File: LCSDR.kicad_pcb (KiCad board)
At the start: 2 copper layers, 100 x 95 mm, 196 parts, among them J1 Conn_01x10, J10 Conn_01x01, J11 Conn_01x01, J2 Conn_01x10, J3 phones, J4 MIC_PTT, J5 Conn_01x10, J6 Conn_Coaxial, J7 Conn_01x10, J8 Conn_01x01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

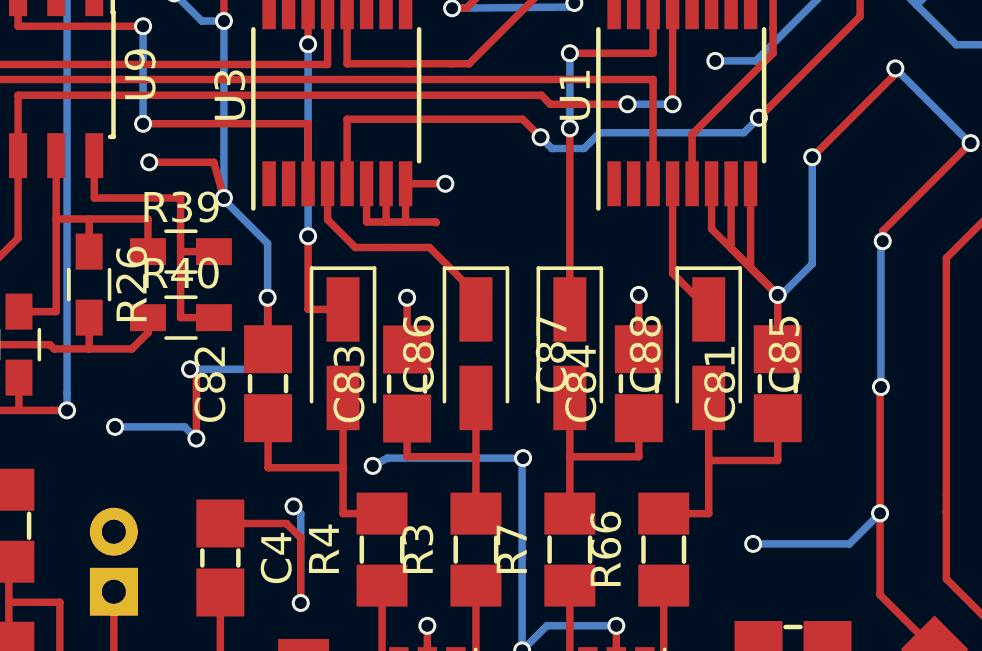
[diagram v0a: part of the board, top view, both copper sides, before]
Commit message: fix PCB distance, right after mixer
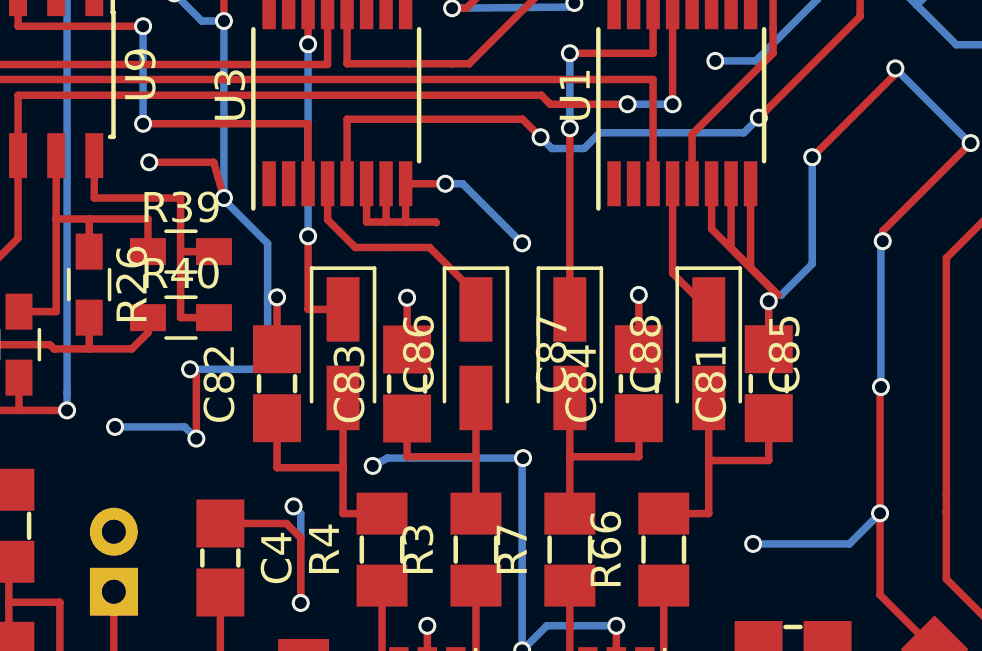
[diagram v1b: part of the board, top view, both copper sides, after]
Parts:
- moved C81 0.30 mm to (180.1, 105.1)
- moved C82 0.30 mm to (163.7, 105.1)
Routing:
- net GND: track 1138.4 -> 1142.1 mm, vias 265 -> 266
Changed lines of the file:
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@@
     (links 414)
     (no_connects 0)
-    (area 114.949999 39.949999 215.050001 135.050001)
+    (area 114.135 38.25238 219.055 136.747619)
     (thickness 1.6)
     (drawings 8)
-    (tracks 1935)
+    (tracks 1939)
     (zones 0)
     (modules 196)
@@
   )
   (module UI:C_1206_0603 (layer F.Cu)
-    (at 180.43 105.14 90)
+    (at 180.13 105.14 90)
     (descr "Capacitor SMD 0603, reflow soldering, AVX (see smccp.pdf)")
     (tags "capacitor 0603")
@@
   )
   (module UI:C_1206_0603 (layer F.Cu)
-    (at 163.44 105.14 90)
+    (at 163.74 105.14 90)
     (descr "Capacitor SMD 0603, reflow soldering, AVX (see smccp.pdf)")
     (tags "capacitor 0603")
@@
   (gr_line (start 116.5 62) (end 116.5 48) (angle 90) (layer Edge.Cuts) (width 0.1))
   (gr_line (start 115 62) (end 116.5 62) (angle 90) (layer Edge.Cuts) (width 0.1))
+  (segment (start 169.35 98.475) (end 169.925 98.475) (width 0.25) (layer B.Cu) (net 1))
+  (via (at 169.35 98.475) (size 0.6) (drill 0.4) (layers F.Cu B.Cu) (net 1))
+  (segment (start 168.025 98.475) (end 169.35 98.475) (width 0.25) (layer F.Cu) (net 1))
+  (via (at 171.91 100.46) (size 0.6) (drill 0.4) (layers F.Cu B.Cu) (net 1))
+  (segment (start 169.925 98.475) (end 171.91 100.46) (width 0.25) (layer B.Cu) (net 1))
+  (segment (start 180.13 103.99) (end 180.13 102.39) (width 0.25) (layer F.Cu) (net 1) (status 400000))
+  (segment (start 180.34 102.18) (end 180.55 102.18) (width 0.25) (layer B.Cu) (net 1))
+  (segment (start 180.13 102.39) (end 180.34 102.18) (width 0.25) (layer B.Cu) (net 1))
+  (via (at 180.13 102.39) (size 0.6) (drill 0.4) (layers F.Cu B.Cu) (net 1))
+  (segment (start 163.74 103.99) (end 163.74 102.26) (width 0.25) (layer F.Cu) (net 1) (status 400000))
+  (via (at 163.74 102.26) (size 0.6) (drill 0.4) (layers F.Cu B.Cu) (net 1))
   (segment (start 180 43) (end 175.45 43) (width 0.25) (layer B.Cu) (net 1))
   (via (at 163.8 46.8) (size 0.6) (drill 0.4) (layers F.Cu B.Cu) (net 1))
@@
   (segment (start 183.84 112.18) (end 185.656827 113.996827) (width 0.25) (layer F.Cu) (net 1))
   (segment (start 180.43 102.18) (end 180.55 102.18) (width 0.25) (layer B.Cu) (net 1))
-  (via (at 180.43 102.18) (size 0.6) (drill 0.4) (layers F.Cu B.Cu) (net 1))
   (segment (start 179.63 110.5) (end 179.69 110.5) (width 0.25) (layer F.Cu) (net 1))
   (segment (start 179.61 110.48) (end 179.63 110.5) (width 0.25) (layer F.Cu) (net 1))
@@
   (segment (start 178.875 100.625) (end 180.43 102.18) (width 0.25) (layer F.Cu) (net 1))
   (segment (start 178.225 98.475) (end 178.225 99.985) (width 0.25) (layer F.Cu) (net 1))
-  (segment (start 180.43 102.18) (end 180.43 103.99) (width 0.25) (layer F.Cu) (net 1))
   (segment (start 180.42 102.18) (end 180.43 102.18) (width 0.25) (layer F.Cu) (net 1))
   (segment (start 178.225 99.985) (end 180.42 102.18) (width 0.25) (layer F.Cu) (net 1))
@@
   (via (at 161.97 93.05) (size 0.6) (drill 0.4) (layers F.Cu B.Cu) (net 1))
   (segment (start 163.425 102.275) (end 163.425 100.465) (width 0.25) (layer B.Cu) (net 1))
-  (segment (start 163.44 102.29) (end 163.425 102.275) (width 0.25) (layer F.Cu) (net 1))
-  (via (at 163.425 102.275) (size 0.6) (drill 0.4) (layers F.Cu B.Cu) (net 1))
-  (segment (start 163.44 103.99) (end 163.44 102.29) (width 0.25) (layer F.Cu) (net 1))
   (segment (start 159.48 97.76) (end 159.48 97.7) (width 0.25) (layer B.Cu) (net 1))
   (via (at 159.48 97.76) (size 0.6) (drill 0.4) (layers F.Cu B.Cu) (net 1))
@@
   (segment (start 168.075 104) (end 168.075 102.275) (width 0.25) (layer F.Cu) (net 1))
   (via (at 168.075 102.275) (size 0.6) (drill 0.4) (layers F.Cu B.Cu) (net 1))
-  (segment (start 168.025 98.475) (end 169.35 98.475) (width 0.25) (layer F.Cu) (net 1))
-  (via (at 169.35 98.475) (size 0.6) (drill 0.4) (layers F.Cu B.Cu) (net 1))
   (segment (start 168.025 98.475) (end 168.025 99.75) (width 0.25) (layer F.Cu) (net 1))
   (segment (start 167.375 99.75) (end 168.025 99.75) (width 0.25) (layer F.Cu) (net 1))
@@
   (segment (start 165.425 94.5) (end 152.5675 94.5) (width 0.25) (layer F.Cu) (net 26))
   (segment (start 165.425 92.575) (end 165.425 94.5) (width 0.25) (layer F.Cu) (net 26))
-  (segment (start 180.43 107.7) (end 178.13 107.7) (width 0.25) (layer F.Cu) (net 27))
-  (segment (start 180.43 106.29) (end 180.43 107.7) (width 0.25) (layer F.Cu) (net 27))
+  (segment (start 180.13 106.29) (end 180.13 107.7) (width 0.25) (layer F.Cu) (net 27))
+  (segment (start 180.13 107.7) (end 178.13 107.7) (width 0.25) (layer F.Cu) (net 27))
   (segment (start 176.63 109.47) (end 178.13 109.47) (width 0.25) (layer F.Cu) (net 27))
   (segment (start 178.13 107.7) (end 178.13 109.47) (width 0.25) (layer F.Cu) (net 27))
@@
   (via (at 159.275 96.475) (size 0.6) (drill 0.4) (layers F.Cu B.Cu) (net 28))
   (segment (start 155.1075 92.1375) (end 155.1075 93.225) (width 0.25) (layer F.Cu) (net 28))
-  (segment (start 163.44 106.29) (end 163.44 107.94) (width 0.25) (layer F.Cu) (net 29))
-  (segment (start 165.94 107.94) (end 163.44 107.94) (width 0.25) (layer F.Cu) (net 29))
+  (segment (start 163.74 106.29) (end 163.74 107.94) (width 0.25) (layer F.Cu) (net 29))
+  (segment (start 165.94 107.94) (end 163.74 107.94) (width 0.25) (layer F.Cu) (net 29))
   (segment (start 165.94 105.615) (end 165.94 107.94) (width 0.25) (layer F.Cu) (net 29))
   (segment (start 165.94 107.94) (end 165.94 109.47) (width 0.25) (layer F.Cu) (net 29))

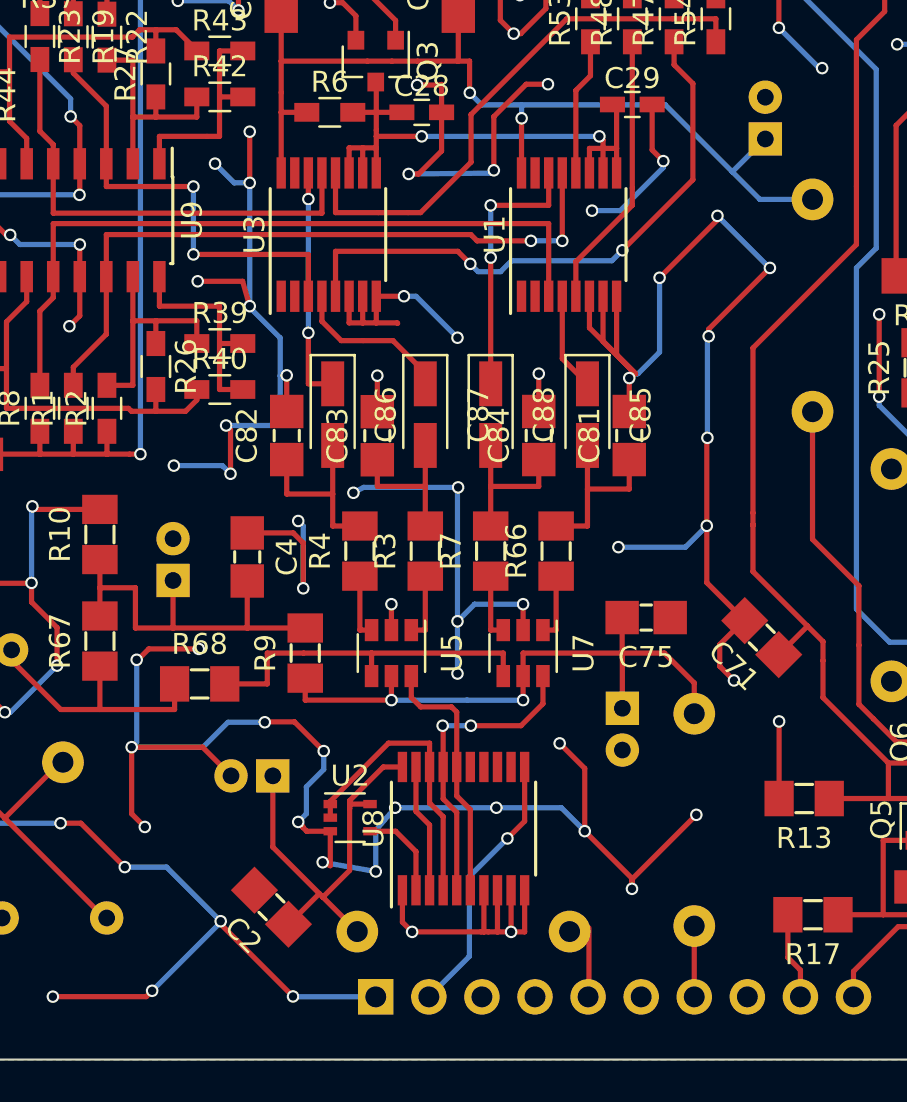
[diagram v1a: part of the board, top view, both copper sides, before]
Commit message: rotate phase with 74LVC74APW
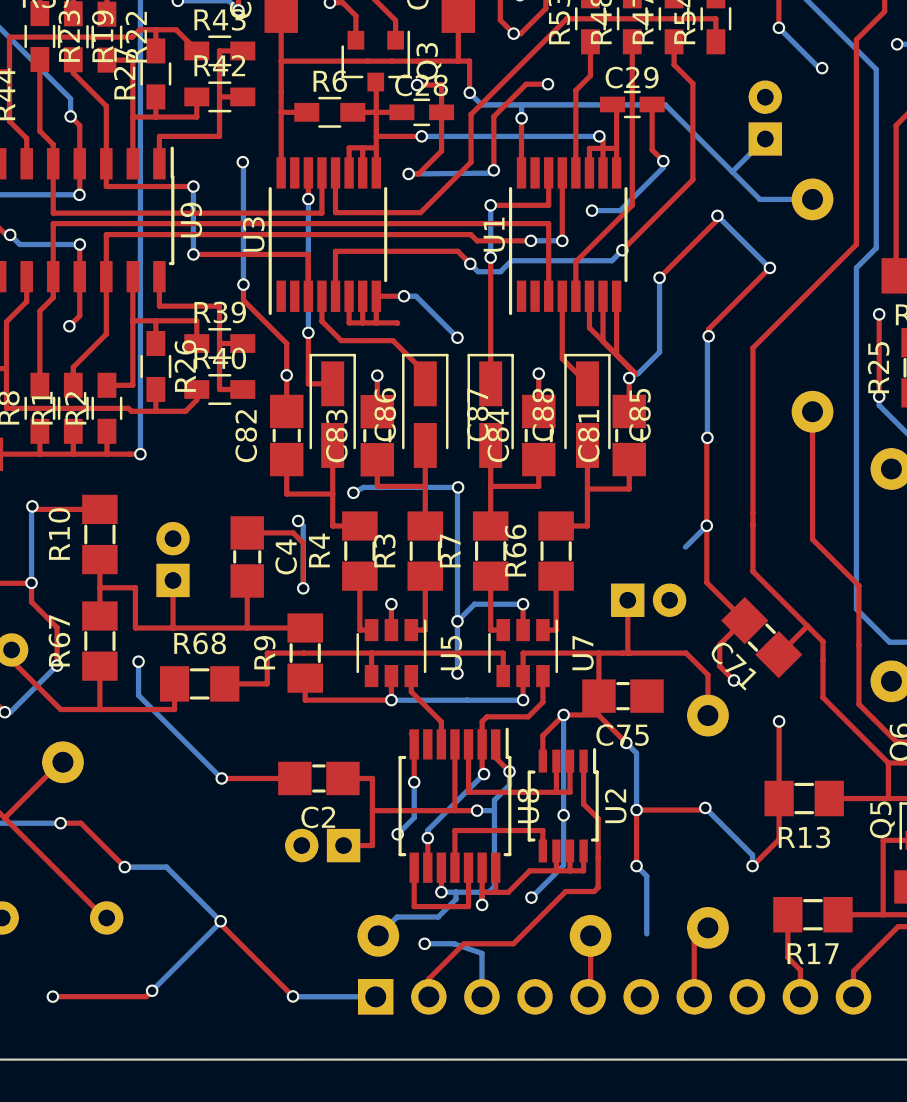
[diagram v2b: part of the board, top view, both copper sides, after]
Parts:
- U2: value 74LVC1G00DCKR -> 74LVC1G74; footprint TO_SOT_Packages_SMD:SOT-353_SC-70-5 -> Housings_SSOP:TSSOP-8_3x3mm_Pitch0.65mm
- U8: value 74LCX574 -> 74LS74; footprint Housings_SSOP:TSSOP-20_4.4x6.5mm_Pitch0.65mm -> Housings_SSOP:TSSOP-14_4.4x5mm_Pitch0.65mm
- moved U2 10.2 mm to (177.0, 122.9), turned to 270 degrees
- moved C2 6.56 mm to (165.3, 121.5), turned to 180 degrees
- moved C76 5.18 mm to (180.1, 113.0), turned to 0 degrees
- moved C3 4.75 mm to (166.5, 124.8)
- moved C75 3.92 mm to (179.8, 117.6)
- moved U8 1.16 mm to (171.8, 122.9), turned to 270 degrees
- moved L1 1.03 mm to (173.3, 129.1)
- moved L10 0.66 mm to (183.9, 123.7)
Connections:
- U2 pad 1: Net-(U2-Pad1) -> CLK
- U2 pad 2: Net-(U2-Pad1) -> Net-(U2-Pad2)
- U2 pad 3: GND -> Net-(U2-Pad2)
- U2 pad 4: Net-(U2-Pad4) -> GND
- U2 pad 5: VCC -> Net-(U2-Pad5)
- U8 pad 1: GND -> VCC
- U8 pad 10: GND -> VCC
- U8 pad 11: CLK -> Net-(U2-Pad5)
- U8 pad 12: (no net) -> Net-(U8-Pad12)
- U8 pad 13: (no net) -> VCC
- U8 pad 14: (no net) -> VCC
- U8 pad 2: Net-(U2-Pad4) -> P90
- U8 pad 3: Net-(U8-Pad19) -> Net-(U2-Pad2)
- U8 pad 4: Net-(U2-Pad1) -> VCC
- U8 pad 5: P90 -> P0
- U8 pad 6: P0 -> (no net)
- U8 pad 8: GND -> Net-(U8-Pad12)
- U8 pad 9: GND -> P90
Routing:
- net GND: track 1142.1 -> 1099.1 mm, vias 266 -> 255
- net VCC: track 21.3 -> 42.7 mm, vias 0 -> 4
- net Net-(U2-Pad1): track 14.0 -> 0.00 mm
- net Net-(U2-Pad2): track 0.00 -> 10.1 mm
- net P0: track 12.3 -> 3.87 mm
- net Net-(U2-Pad5): track 0.00 -> 6.96 mm
- net Net-(U8-Pad12): track 0.00 -> 6.32 mm
- net Net-(U8-Pad19): track 6.17 -> 0.00 mm
- net Net-(U2-Pad4): track 4.45 -> 0.00 mm
- net CLK: track 13.5 -> 17.7 mm, vias 1 -> 0
- net P90: track 14.7 -> 12.7 mm
- net Net-(C75-Pad2): track 29.5 -> 30.9 mm

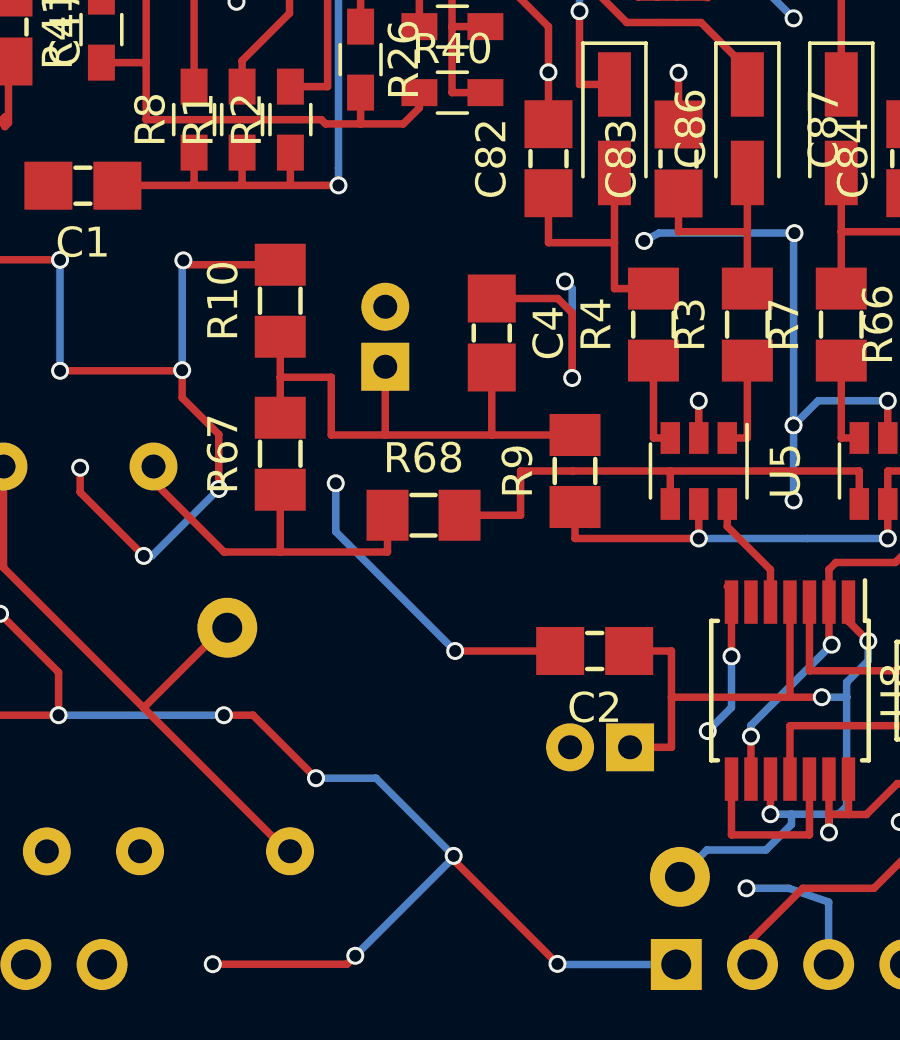
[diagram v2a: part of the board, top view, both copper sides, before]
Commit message: add gnd vias
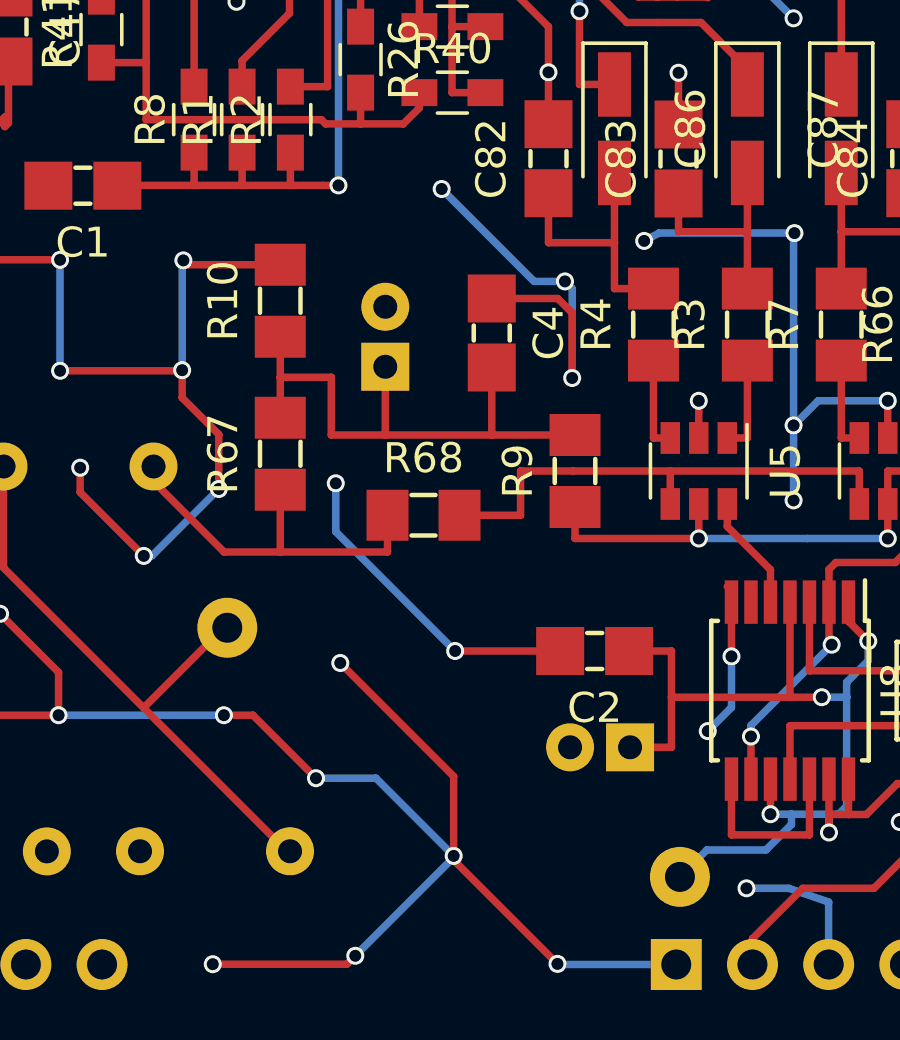
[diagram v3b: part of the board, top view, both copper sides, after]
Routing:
- net GND: track 1099.1 -> 1112.6 mm, vias 255 -> 257
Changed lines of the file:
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@@
     (thickness 1.6)
     (drawings 8)
-    (tracks 1916)
+    (tracks 1924)
     (zones 0)
     (modules 196)
@@
   (gr_line (start 116.5 62) (end 116.5 48) (angle 90) (layer Edge.Cuts) (width 0.1))
   (gr_line (start 115 62) (end 116.5 62) (angle 90) (layer Edge.Cuts) (width 0.1))
-  (segment (start 164.13 121.55) (end 160.63 121.55) (width 0.25) (layer F.Cu) (net 1) (status 400000))
+  (segment (start 164.29 109.23) (end 163.26 109.23) (width 0.25) (layer B.Cu) (net 1))
+  (via (at 160.18 106.15) (size 0.6) (drill 0.4) (layers F.Cu B.Cu) (net 1))
+  (segment (start 163.26 109.23) (end 160.18 106.15) (width 0.25) (layer B.Cu) (net 1))
+  (segment (start 160.58 128.38) (end 160.58 125.73) (width 0.25) (layer F.Cu) (net 1))
+  (segment (start 156.82 121.93) (end 156.82 121.84) (width 0.25) (layer B.Cu) (net 1))
+  (segment (start 156.8 121.95) (end 156.82 121.93) (width 0.25) (layer B.Cu) (net 1))
+  (via (at 156.8 121.95) (size 0.6) (drill 0.4) (layers F.Cu B.Cu) (net 1))
+  (segment (start 160.58 125.73) (end 156.8 121.95) (width 0.25) (layer F.Cu) (net 1))
+  (segment (start 164.13 121.55) (end 160.63 121.55) (width 0.25) (layer F.Cu) (net 1))
   (via (at 156.65 115.96) (size 0.6) (drill 0.4) (layers F.Cu B.Cu) (net 1))
   (segment (start 156.65 117.57) (end 156.65 115.96) (width 0.25) (layer B.Cu) (net 1))
@@
   (via (at 173.09 127.6) (size 0.6) (drill 0.4) (layers F.Cu B.Cu) (net 46))
   (via (at 171.14 126.99) (size 0.6) (drill 0.4) (layers F.Cu B.Cu) (net 46))
-  (segment (start 178.68 117.61) (end 178.68 115.55) (width 0.25) (layer F.Cu) (net 47) (status 400000))
-  (segment (start 180.06 113.02) (end 180.06 115.55) (width 0.25) (layer F.Cu) (net 47) (status 400000))
+  (segment (start 178.68 117.61) (end 178.68 115.55) (width 0.25) (layer F.Cu) (net 47))
+  (segment (start 180.06 113.02) (end 180.06 115.55) (width 0.25) (layer F.Cu) (net 47))
   (segment (start 180.16 115.55) (end 180.06 115.55) (width 0.25) (layer F.Cu) (net 47))
   (segment (start 180.06 115.55) (end 182.85 115.55) (width 0.25) (layer F.Cu) (net 47))
